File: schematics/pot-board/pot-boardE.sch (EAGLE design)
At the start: 15 parts, among them J3 POWER_JACKPTH_LOCK, U1 SPARKFUN_PRO_MICRO, U2 DC-DC-STEP-DOWN-LM2596

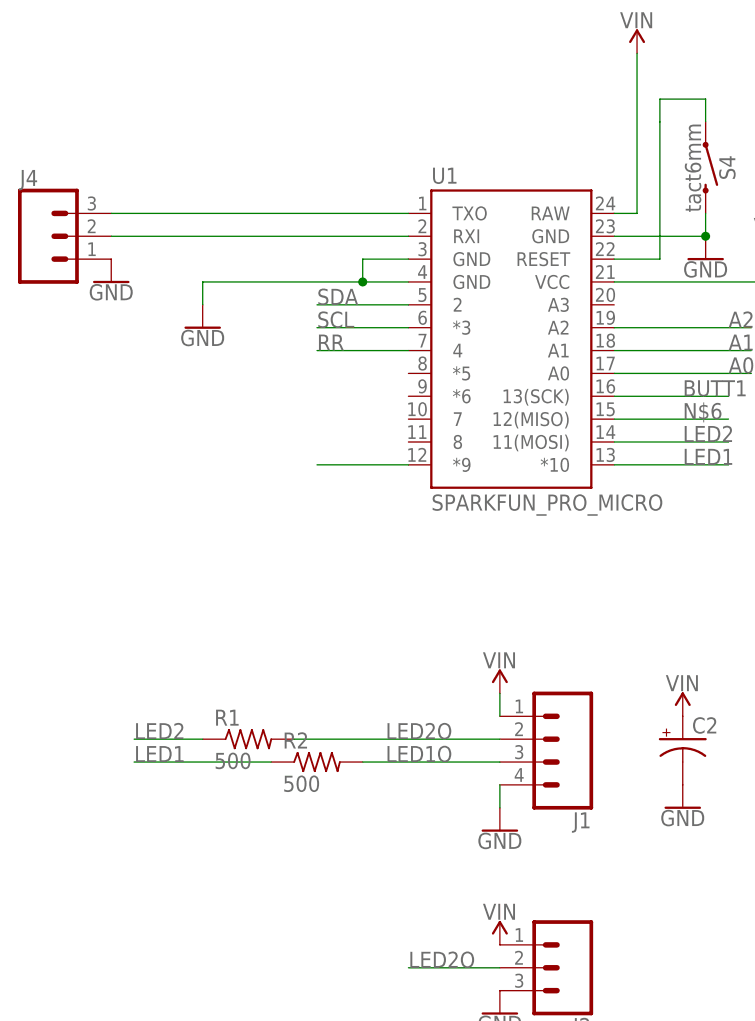
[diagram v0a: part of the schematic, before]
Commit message: added variations up to woodArc1 using pot-boardE
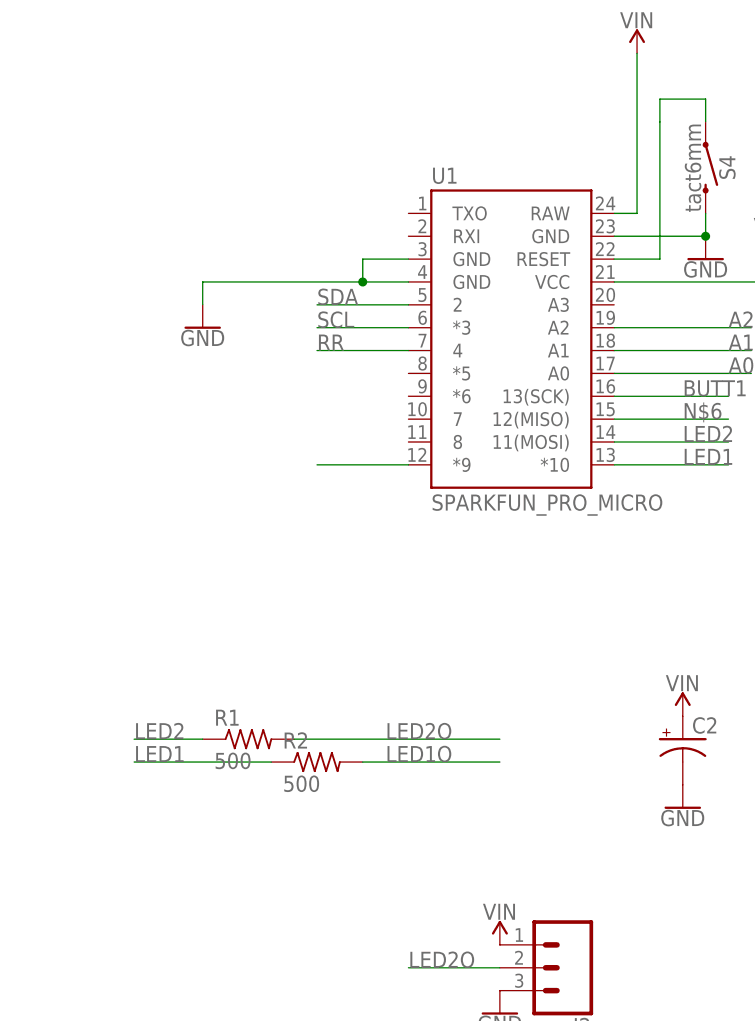
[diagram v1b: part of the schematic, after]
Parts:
- removed J1: (no value), SparkFun-Connectors:CONN_04
- removed J4: (no value), SparkFun-Connectors:CONN_03
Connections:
- removed net N$3: J4.2, U1.RXI
- removed net N$4: J4.3, U1.TXO
- net GND: no longer J1.4, J4.1
- net LED1O: no longer J1.3
- net LED2O: no longer J1.2
- net VIN: no longer J1.1
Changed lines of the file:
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@@
 <part name="SUPPLY1" library="SparkFun-PowerSymbols" deviceset="VCC" device=""/>
 <part name="GND5" library="SparkFun-PowerSymbols" deviceset="GND" device=""/>
-<part name="GND7" library="SparkFun-PowerSymbols" deviceset="GND" device=""/>
-<part name="SUPPLY4" library="SparkFun-PowerSymbols" deviceset="VIN" device=""/>
 <part name="J3" library="SparkFun-Connectors" deviceset="POWER_JACK" device="PTH_LOCK"/>
 <part name="GND8" library="SparkFun-PowerSymbols" deviceset="GND" device=""/>
 <part name="S4" library="SparkFun-Switches" deviceset="MOMENTARY-SWITCH-SPST" device="-PTH-6.0MM" value="tact6mm"/>
 <part name="SUPPLY5" library="SparkFun-PowerSymbols" deviceset="VIN" device=""/>
-<part name="J4" library="SparkFun-Connectors" deviceset="CONN_03" device=""/>
-<part name="GND10" library="SparkFun-PowerSymbols" deviceset="GND" device=""/>
 <part name="SUPPLY6" library="SparkFun-PowerSymbols" deviceset="VIN" device=""/>
 <part name="GND11" library="SparkFun-PowerSymbols" deviceset="GND" device=""/>
@@
 <part name="S1" library="SparkFun-Switches" deviceset="MOMENTARY-SWITCH-SPST" device="-PTH-6.0MM" value="tact6mm"/>
 <part name="GND9" library="SparkFun-PowerSymbols" deviceset="GND" device=""/>
-<part name="J1" library="SparkFun-Connectors" deviceset="CONN_04" device=""/>
 <part name="J2" library="SparkFun-Connectors" deviceset="CONN_03" device=""/>
 <part name="J5" library="SparkFun-Connectors" deviceset="CONN_03" device=""/>
@@
 <instance part="SUPPLY1" gate="G$1" x="53.34" y="78.74"/>
 <instance part="GND5" gate="1" x="45.72" y="78.74"/>
-<instance part="GND7" gate="1" x="22.86" y="15.24"/>
-<instance part="SUPPLY4" gate="G$1" x="22.86" y="30.48"/>
 <instance part="J3" gate="G$1" x="104.14" y="12.7" rot="MR0"/>
 <instance part="GND8" gate="1" x="101.6" y="10.16"/>
 <instance part="S4" gate="G$1" x="45.72" y="88.9" rot="R270"/>
 <instance part="SUPPLY5" gate="G$1" x="38.1" y="101.6"/>
-<instance part="J4" gate="J$1" x="-27.94" y="81.28"/>
-<instance part="GND10" gate="1" x="-20.32" y="76.2"/>
 <instance part="SUPPLY6" gate="G$1" x="43.18" y="27.94"/>
 <instance part="GND11" gate="1" x="43.18" y="17.78"/>
@@
 <instance part="S1" gate="G$1" x="78.74" y="93.98" rot="R270"/>
 <instance part="GND9" gate="1" x="78.74" y="86.36"/>
-<instance part="J1" gate="G$1" x="27.94" y="25.4" rot="R180"/>
 <instance part="J2" gate="J$1" x="30.48" y="0" rot="R180"/>
 <instance part="J5" gate="J$1" x="30.48" y="-17.78" rot="R180"/>
@@
 </segment>
 <segment>
-<pinref part="GND7" gate="1" pin="GND"/>
-<pinref part="J1" gate="G$1" pin="4"/>
-<wire x1="22.86" y1="17.78" x2="22.86" y2="20.32" width="0.1524" layer="91"/>
-</segment>
-<segment>
 <pinref part="J3" gate="G$1" pin="GNDBREAK"/>
 <pinref part="J3" gate="G$1" pin="GND"/>
@@
 <junction x="101.6" y="15.24"/>
 <wire x1="101.6" y1="15.24" x2="101.6" y2="12.7" width="0.1524" layer="91"/>
-</segment>
-<segment>
-<pinref part="J4" gate="J$1" pin="1"/>
-<pinref part="GND10" gate="1" pin="GND"/>
 </segment>
 <segment>
@@
 </segment>
 <segment>
-<pinref part="J1" gate="G$1" pin="1"/>
-<pinref part="SUPPLY4" gate="G$1" pin="VIN"/>
-<wire x1="22.86" y1="27.94" x2="22.86" y2="30.48" width="0.1524" layer="91"/>
-</segment>
-<segment>
 <pinref part="J2" gate="J$1" pin="1"/>
 <pinref part="SUPPLY3" gate="G$1" pin="VIN"/>
@@
 </segment>
 </net>
-<net name="N$3" class="0">
-<segment>
-<pinref part="U1" gate="G$1" pin="RXI"/>
-<pinref part="J4" gate="J$1" pin="2"/>
-<wire x1="12.7" y1="81.28" x2="-20.32" y2="81.28" width="0.1524" layer="91"/>
-</segment>
-</net>
-<net name="N$4" class="0">
-<segment>
-<pinref part="U1" gate="G$1" pin="TXO"/>
-<pinref part="J4" gate="J$1" pin="3"/>
-<wire x1="12.7" y1="83.82" x2="-20.32" y2="83.82" width="0.1524" layer="91"/>
-</segment>
-</net>
 <net name="A0" class="0">
 <segment>
@@
 <net name="LED1O" class="0">
 <segment>
-<pinref part="J1" gate="G$1" pin="3"/>
 <wire x1="22.86" y1="22.86" x2="7.62" y2="22.86" width="0.1524" layer="91"/>
 <label x="10.16" y="22.86" size="1.778" layer="95"/>
@@
 <net name="LED2O" class="0">
 <segment>
-<pinref part="J1" gate="G$1" pin="2"/>
 <wire x1="22.86" y1="25.4" x2="0" y2="25.4" width="0.1524" layer="91"/>
 <label x="10.16" y="25.4" size="1.778" layer="95"/>
